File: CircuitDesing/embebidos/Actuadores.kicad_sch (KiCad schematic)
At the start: 18 parts

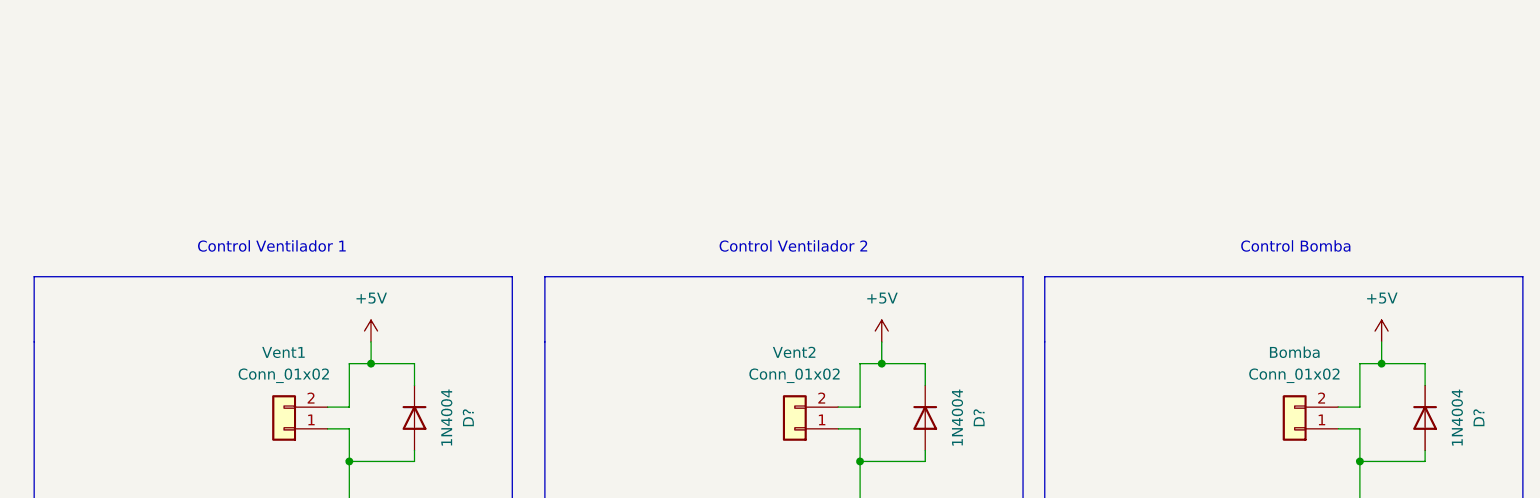
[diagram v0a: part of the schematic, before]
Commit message: Potencia
Primera propuesta del esquema de potencia
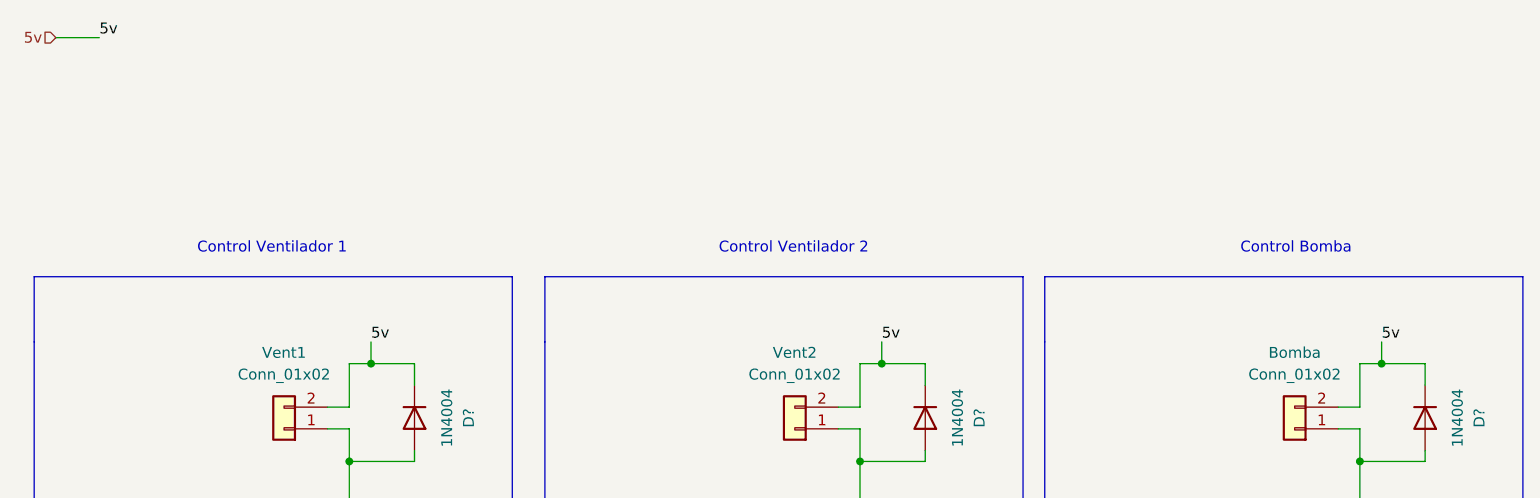
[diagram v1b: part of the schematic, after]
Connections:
- net +5V renamed 5v
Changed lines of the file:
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@@
+    (stroke (width 0) (type default) (color 0 0 0 0))
+  )
+  (wire (pts (xy 64.77 40.64) (xy 69.85 40.64))
     (stroke (width 0) (type default) (color 0 0 0 0))
   )
@@
   )
   (text "Control Ventilador 2" (at 142.24 66.04 0)
+    (effects (font (size 1.27 1.27)) (justify left bottom))
+  )
+  (label "5v" (at 161.29 76.2 0)
+    (effects (font (size 1.27 1.27)) (justify left bottom))
+  )
+  (label "5v" (at 219.71 76.2 0)
+    (effects (font (size 1.27 1.27)) (justify left bottom))
+  )
+  (label "5v" (at 101.6 76.2 0)
+    (effects (font (size 1.27 1.27)) (justify left bottom))
+  )
+  (label "5v" (at 69.85 40.64 0)
     (effects (font (size 1.27 1.27)) (justify left bottom))
   )
@@
   )
   (hierarchical_label "C_Vent2" (shape input) (at 133.35 95.25 180)
+    (effects (font (size 1.27 1.27)) (justify right))
+  )
+  (hierarchical_label "5v" (shape input) (at 64.77 40.64 180)
     (effects (font (size 1.27 1.27)) (justify right))
   )
@@
     (pin "2")
   )
-  (symbol (lib_id "power:+5V") (at 101.6 76.2 0) (unit 1)
-    (in_bom yes) (on_board yes) (fields_autoplaced)
-    (property "Reference" "#PWR?" (id 0) (at 101.6 80.01 0)
-      (effects (font (size 1.27 1.27)) hide)
-    )
-    (property "Value" "+5V" (id 1) (at 101.6 71.12 0))
-    (property "Footprint" "" (id 2) (at 101.6 76.2 0)
-      (effects (font (size 1.27 1.27)) hide)
-    )
-    (property "Datasheet" "" (id 3) (at 101.6 76.2 0)
-      (effects (font (size 1.27 1.27)) hide)
-    )
-    (pin "1")
-  )
   (symbol (lib_id "power:GND") (at 147.32 118.11 0) (unit 1)
     (in_bom yes) (on_board yes) (fields_autoplaced)
@@
     (pin "3")
   )
-  (symbol (lib_id "power:+5V") (at 219.71 76.2 0) (unit 1)
-    (in_bom yes) (on_board yes) (fields_autoplaced)
-    (property "Reference" "#PWR?" (id 0) (at 219.71 80.01 0)
-      (effects (font (size 1.27 1.27)) hide)
-    )
-    (property "Value" "+5V" (id 1) (at 219.71 71.12 0))
-    (property "Footprint" "" (id 2) (at 219.71 76.2 0)
-      (effects (font (size 1.27 1.27)) hide)
-    )
-    (property "Datasheet" "" (id 3) (at 219.71 76.2 0)
-      (effects (font (size 1.27 1.27)) hide)
-    )
-    (pin "1")
-  )
   (symbol (lib_id "Diode:1N4004") (at 106.68 85.09 270) (unit 1)
     (in_bom yes) (on_board yes) (fields_autoplaced)
@@
     (pin "2")
   )
-  (symbol (lib_id "power:+5V") (at 161.29 76.2 0) (unit 1)
-    (in_bom yes) (on_board yes) (fields_autoplaced)
-    (property "Reference" "#PWR?" (id 0) (at 161.29 80.01 0)
-      (effects (font (size 1.27 1.27)) hide)
-    )
-    (property "Value" "+5V" (id 1) (at 161.29 71.12 0))
-    (property "Footprint" "" (id 2) (at 161.29 76.2 0)
-      (effects (font (size 1.27 1.27)) hide)
-    )
-    (property "Datasheet" "" (id 3) (at 161.29 76.2 0)
-      (effects (font (size 1.27 1.27)) hide)
-    )
-    (pin "1")
-  )
   (symbol (lib_id "power:GND") (at 77.47 119.38 0) (unit 1)

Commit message: LDR
Comparacion LDR
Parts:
- R: renamed from R?; value R -> (none)
- R? (x5): value R -> (none)
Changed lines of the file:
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@@
       (effects (font (size 1.27 1.27)) (justify left))
     )
-    (property "Value" "R" (id 1) (at 90.17 107.9499 0)
+    (property "Value" "" (id 1) (at 90.17 107.9499 0)
       (effects (font (size 1.27 1.27)) (justify left))
     )
@@
   (symbol (lib_id "Device:R") (at 77.47 109.22 0) (unit 1)
     (in_bom yes) (on_board yes) (fields_autoplaced)
-    (property "Reference" "R?" (id 0) (at 80.01 107.9499 0)
-      (effects (font (size 1.27 1.27)) (justify left))
-    )
-    (property "Value" "R" (id 1) (at 80.01 110.4899 0)
+    (property "Reference" "R" (id 0) (at 80.01 107.9499 0)
+      (effects (font (size 1.27 1.27)) (justify left))
+    )
+    (property "Value" "" (id 1) (at 80.01 110.4899 0)
       (effects (font (size 1.27 1.27)) (justify left))
     )
@@
       (effects (font (size 1.27 1.27)) (justify left))
     )
-    (property "Value" "R" (id 1) (at 139.7 110.4899 0)
+    (property "Value" "" (id 1) (at 139.7 110.4899 0)
       (effects (font (size 1.27 1.27)) (justify left))
     )
@@
       (effects (font (size 1.27 1.27)) (justify left))
     )
-    (property "Value" "R" (id 1) (at 198.12 110.4899 0)
+    (property "Value" "" (id 1) (at 198.12 110.4899 0)
       (effects (font (size 1.27 1.27)) (justify left))
     )
@@
       (effects (font (size 1.27 1.27)) (justify left))
     )
-    (property "Value" "R" (id 1) (at 149.86 107.9499 0)
+    (property "Value" "" (id 1) (at 149.86 107.9499 0)
       (effects (font (size 1.27 1.27)) (justify left))
     )
@@
       (effects (font (size 1.27 1.27)) (justify left))
     )
-    (property "Value" "R" (id 1) (at 208.28 107.9499 0)
-      (effects (font (size 1.27 1.27)) (justify left))
-    )
+    (property "Value" "" (id 1) (at 208.28 107.9499 0)
+      (effects (font (size 1.27 1.27)) (justify left))
+    )

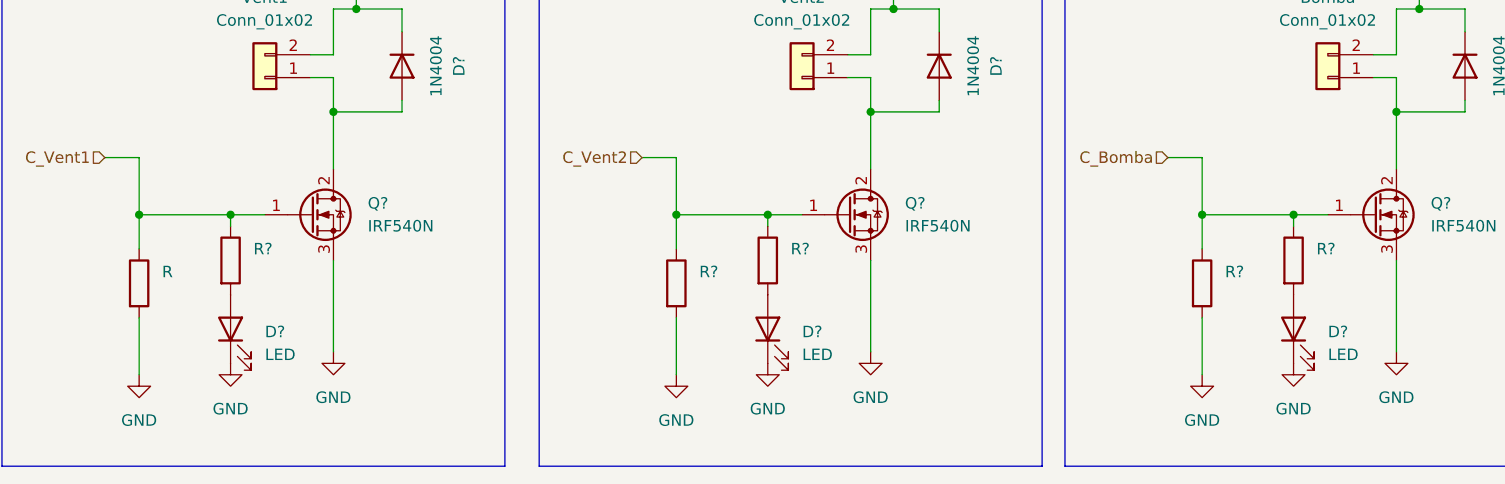
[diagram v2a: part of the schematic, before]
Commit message: Sensor Ultrasonido
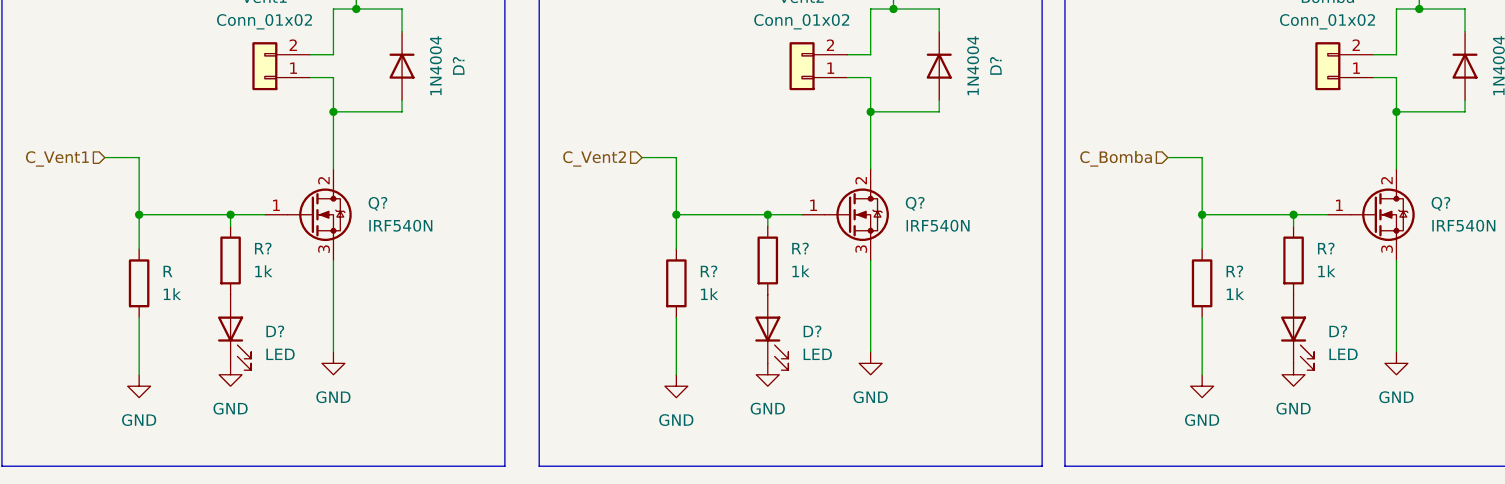
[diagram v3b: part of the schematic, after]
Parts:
- R, R? (x5): value (none) -> 1k
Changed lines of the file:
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@@
       (effects (font (size 1.27 1.27)) (justify left))
     )
-    (property "Value" "" (id 1) (at 90.17 107.9499 0)
+    (property "Value" "1k" (id 1) (at 90.17 107.9499 0)
       (effects (font (size 1.27 1.27)) (justify left))
     )
@@
       (effects (font (size 1.27 1.27)) (justify left))
     )
-    (property "Value" "" (id 1) (at 80.01 110.4899 0)
+    (property "Value" "1k" (id 1) (at 80.01 110.4899 0)
       (effects (font (size 1.27 1.27)) (justify left))
     )
@@
       (effects (font (size 1.27 1.27)) (justify left))
     )
-    (property "Value" "" (id 1) (at 139.7 110.4899 0)
+    (property "Value" "1k" (id 1) (at 139.7 110.4899 0)
       (effects (font (size 1.27 1.27)) (justify left))
     )
@@
       (effects (font (size 1.27 1.27)) (justify left))
     )
-    (property "Value" "" (id 1) (at 198.12 110.4899 0)
+    (property "Value" "1k" (id 1) (at 198.12 110.4899 0)
       (effects (font (size 1.27 1.27)) (justify left))
     )
@@
       (effects (font (size 1.27 1.27)) (justify left))
     )
-    (property "Value" "" (id 1) (at 149.86 107.9499 0)
+    (property "Value" "1k" (id 1) (at 149.86 107.9499 0)
       (effects (font (size 1.27 1.27)) (justify left))
     )
@@
       (effects (font (size 1.27 1.27)) (justify left))
     )
-    (property "Value" "" (id 1) (at 208.28 107.9499 0)
-      (effects (font (size 1.27 1.27)) (justify left))
-    )
+    (property "Value" "1k" (id 1) (at 208.28 107.9499 0)
+      (effects (font (size 1.27 1.27)) (justify left))
+    )

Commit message: Huellas parciales
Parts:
- Bomba1: renamed from Bomba; footprint (none) -> Connector_JST:JST_EH_B2B-EH-A_1x02_P2.50mm_Vertical
- gave numbers to parts that had none: 14
- renumbered R to R2
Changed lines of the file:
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@@
   (symbol (lib_id "Device:R") (at 87.63 106.68 0) (unit 1)
     (in_bom yes) (on_board yes) (fields_autoplaced)
-    (property "Reference" "R?" (id 0) (at 90.17 105.4099 0)
+    (property "Reference" "R3" (id 0) (at 90.17 105.4099 0)
       (effects (font (size 1.27 1.27)) (justify left))
     )
@@
   (symbol (lib_id "Device:LED") (at 147.32 114.3 90) (unit 1)
     (in_bom yes) (on_board yes) (fields_autoplaced)
-    (property "Reference" "D?" (id 0) (at 151.13 114.6174 90)
+    (property "Reference" "D8" (id 0) (at 151.13 114.6174 90)
       (effects (font (size 1.27 1.27)) (justify right))
     )
@@
   (symbol (lib_id "Device:R") (at 77.47 109.22 0) (unit 1)
     (in_bom yes) (on_board yes) (fields_autoplaced)
-    (property "Reference" "R" (id 0) (at 80.01 107.9499 0)
+    (property "Reference" "R2" (id 0) (at 80.01 107.9499 0)
       (effects (font (size 1.27 1.27)) (justify left))
     )
@@
   (symbol (lib_id "Transistor_FET:IRF540N") (at 96.52 101.6 0) (unit 1)
     (in_bom yes) (on_board yes) (fields_autoplaced)
-    (property "Reference" "Q?" (id 0) (at 102.87 100.3299 0)
+    (property "Reference" "Q1" (id 0) (at 102.87 100.3299 0)
       (effects (font (size 1.27 1.27)) (justify left))
     )
@@
   (symbol (lib_id "Device:LED") (at 87.63 114.3 90) (unit 1)
     (in_bom yes) (on_board yes) (fields_autoplaced)
-    (property "Reference" "D?" (id 0) (at 91.44 114.6174 90)
+    (property "Reference" "D6" (id 0) (at 91.44 114.6174 90)
       (effects (font (size 1.27 1.27)) (justify right))
     )
@@
   (symbol (lib_id "power:GND") (at 137.16 119.38 0) (unit 1)
     (in_bom yes) (on_board yes) (fields_autoplaced)
-    (property "Reference" "#PWR?" (id 0) (at 137.16 125.73 0)
+    (property "Reference" "#PWR010" (id 0) (at 137.16 125.73 0)
       (effects (font (size 1.27 1.27)) hide)
     )
@@
   (symbol (lib_id "Connector_Generic:Conn_01x02") (at 209.55 86.36 180) (unit 1)
     (in_bom yes) (on_board yes) (fields_autoplaced)
-    (property "Reference" "Bomba" (id 0) (at 209.55 77.47 0))
+    (property "Reference" "Bomba1" (id 0) (at 209.55 77.47 0))
     (property "Value" "Conn_01x02" (id 1) (at 209.55 80.01 0))
-    (property "Footprint" "" (id 2) (at 209.55 86.36 0)
+    (property "Footprint" "Connector_JST:JST_EH_B2B-EH-A_1x02_P2.50mm_Vertical" (id 2) (at 209.55 86.36 0)
       (effects (font (size 1.27 1.27)) hide)
     )
@@
   (symbol (lib_id "power:GND") (at 147.32 118.11 0) (unit 1)
     (in_bom yes) (on_board yes) (fields_autoplaced)
-    (property "Reference" "#PWR?" (id 0) (at 147.32 124.46 0)
+    (property "Reference" "#PWR011" (id 0) (at 147.32 124.46 0)
       (effects (font (size 1.27 1.27)) hide)
     )
@@
   (symbol (lib_id "Device:LED") (at 205.74 114.3 90) (unit 1)
     (in_bom yes) (on_board yes) (fields_autoplaced)
-    (property "Reference" "D?" (id 0) (at 209.55 114.6174 90)
+    (property "Reference" "D10" (id 0) (at 209.55 114.6174 90)
       (effects (font (size 1.27 1.27)) (justify right))
     )
@@
   (symbol (lib_id "power:GND") (at 87.63 118.11 0) (unit 1)
     (in_bom yes) (on_board yes) (fields_autoplaced)
-    (property "Reference" "#PWR?" (id 0) (at 87.63 124.46 0)
+    (property "Reference" "#PWR08" (id 0) (at 87.63 124.46 0)
       (effects (font (size 1.27 1.27)) hide)
     )
@@
   (symbol (lib_id "power:GND") (at 205.74 118.11 0) (unit 1)
     (in_bom yes) (on_board yes) (fields_autoplaced)
-    (property "Reference" "#PWR?" (id 0) (at 205.74 124.46 0)
+    (property "Reference" "#PWR014" (id 0) (at 205.74 124.46 0)
       (effects (font (size 1.27 1.27)) hide)
     )
@@
   (symbol (lib_id "power:GND") (at 158.75 116.84 0) (unit 1)
     (in_bom yes) (on_board yes) (fields_autoplaced)
-    (property "Reference" "#PWR?" (id 0) (at 158.75 123.19 0)
+    (property "Reference" "#PWR012" (id 0) (at 158.75 123.19 0)
       (effects (font (size 1.27 1.27)) hide)
     )
@@
   (symbol (lib_id "Transistor_FET:IRF540N") (at 156.21 101.6 0) (unit 1)
     (in_bom yes) (on_board yes) (fields_autoplaced)
-    (property "Reference" "Q?" (id 0) (at 162.56 100.3299 0)
+    (property "Reference" "Q2" (id 0) (at 162.56 100.3299 0)
       (effects (font (size 1.27 1.27)) (justify left))
     )
@@
   (symbol (lib_id "Device:R") (at 137.16 109.22 0) (unit 1)
     (in_bom yes) (on_board yes) (fields_autoplaced)
-    (property "Reference" "R?" (id 0) (at 139.7 107.9499 0)
+    (property "Reference" "R4" (id 0) (at 139.7 107.9499 0)
       (effects (font (size 1.27 1.27)) (justify left))
     )
@@
   (symbol (lib_id "Device:R") (at 195.58 109.22 0) (unit 1)
     (in_bom yes) (on_board yes) (fields_autoplaced)
-    (property "Reference" "R?" (id 0) (at 198.12 107.9499 0)
+    (property "Reference" "R6" (id 0) (at 198.12 107.9499 0)
       (effects (font (size 1.27 1.27)) (justify left))
     )
@@
   (symbol (lib_id "Diode:1N4004") (at 166.37 85.09 270) (unit 1)
     (in_bom yes) (on_board yes) (fields_autoplaced)
-    (property "Reference" "D?" (id 0) (at 172.72 85.09 0))
+    (property "Reference" "D9" (id 0) (at 172.72 85.09 0))
     (property "Value" "1N4004" (id 1) (at 170.18 85.09 0))
     (property "Footprint" "Diode_THT:D_DO-41_SOD81_P10.16mm_Horizontal" (id 2) (at 161.925 85.09 0)
@@
   (symbol (lib_id "Device:R") (at 147.32 106.68 0) (unit 1)
     (in_bom yes) (on_board yes) (fields_autoplaced)
-    (property "Reference" "R?" (id 0) (at 149.86 105.4099 0)
+    (property "Reference" "R5" (id 0) (at 149.86 105.4099 0)
       (effects (font (size 1.27 1.27)) (justify left))
     )
@@
   (symbol (lib_id "Device:R") (at 205.74 106.68 0) (unit 1)
     (in_bom yes) (on_board yes) (fields_autoplaced)
-    (property "Reference" "R?" (id 0) (at 208.28 105.4099 0)
+    (property "Reference" "R7" (id 0) (at 208.28 105.4099 0)
       (effects (font (size 1.27 1.27)) (justify left))
     )
@@
   (symbol (lib_id "power:GND") (at 195.58 119.38 0) (unit 1)
     (in_bom yes) (on_board yes) (fields_autoplaced)
-    (property "Reference" "#PWR?" (id 0) (at 195.58 125.73 0)
+    (property "Reference" "#PWR013" (id 0) (at 195.58 125.73 0)
       (effects (font (size 1.27 1.27)) hide)
     )
@@
   (symbol (lib_id "power:GND") (at 99.06 116.84 0) (unit 1)
     (in_bom yes) (on_board yes) (fields_autoplaced)
-    (property "Reference" "#PWR?" (id 0) (at 99.06 123.19 0)
+    (property "Reference" "#PWR09" (id 0) (at 99.06 123.19 0)
       (effects (font (size 1.27 1.27)) hide)
     )
@@
   (symbol (lib_id "Diode:1N4004") (at 224.79 85.09 270) (unit 1)
     (in_bom yes) (on_board yes) (fields_autoplaced)
-    (property "Reference" "D?" (id 0) (at 231.14 85.09 0))
+    (property "Reference" "D11" (id 0) (at 231.14 85.09 0))
     (property "Value" "1N4004" (id 1) (at 228.6 85.09 0))
     (property "Footprint" "Diode_THT:D_DO-41_SOD81_P10.16mm_Horizontal" (id 2) (at 220.345 85.09 0)
@@
   (symbol (lib_id "Transistor_FET:IRF540N") (at 214.63 101.6 0) (unit 1)
     (in_bom yes) (on_board yes) (fields_autoplaced)
-    (property "Reference" "Q?" (id 0) (at 220.98 100.3299 0)
+    (property "Reference" "Q3" (id 0) (at 220.98 100.3299 0)
       (effects (font (size 1.27 1.27)) (justify left))
     )
@@
   (symbol (lib_id "Diode:1N4004") (at 106.68 85.09 270) (unit 1)
     (in_bom yes) (on_board yes) (fields_autoplaced)
-    (property "Reference" "D?" (id 0) (at 113.03 85.09 0))
+    (property "Reference" "D7" (id 0) (at 113.03 85.09 0))
     (property "Value" "1N4004" (id 1) (at 110.49 85.09 0))
     (property "Footprint" "Diode_THT:D_DO-41_SOD81_P10.16mm_Horizontal" (id 2) (at 102.235 85.09 0)
@@
   (symbol (lib_id "power:GND") (at 77.47 119.38 0) (unit 1)
     (in_bom yes) (on_board yes) (fields_autoplaced)
-    (property "Reference" "#PWR?" (id 0) (at 77.47 125.73 0)
+    (property "Reference" "#PWR07" (id 0) (at 77.47 125.73 0)
       (effects (font (size 1.27 1.27)) hide)
     )
@@
   (symbol (lib_id "power:GND") (at 217.17 116.84 0) (unit 1)
     (in_bom yes) (on_board yes) (fields_autoplaced)
-    (property "Reference" "#PWR?" (id 0) (at 217.17 123.19 0)
-      (effects (font (size 1.27 1.27)) hide)
-    )
+    (property "Reference" "#PWR015" (id 0) (at 217.17 123.19 0)
+      (effects (font (size 1.27 1.27)) hide)
+    )

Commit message: 15 footprints faltantes
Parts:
- R2, R3, R4, R5, R6, R7: footprint (none) -> Resistor_SMD:R_0603_1608Metric_Pad0.98x0.95mm_HandSolder
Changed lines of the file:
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@@
       (effects (font (size 1.27 1.27)) (justify left))
     )
-    (property "Footprint" "" (id 2) (at 85.852 106.68 90)
+    (property "Footprint" "Resistor_SMD:R_0603_1608Metric_Pad0.98x0.95mm_HandSolder" (id 2) (at 85.852 106.68 90)
       (effects (font (size 1.27 1.27)) hide)
     )
@@
       (effects (font (size 1.27 1.27)) (justify left))
     )
-    (property "Footprint" "" (id 2) (at 75.692 109.22 90)
+    (property "Footprint" "Resistor_SMD:R_0603_1608Metric_Pad0.98x0.95mm_HandSolder" (id 2) (at 75.692 109.22 90)
       (effects (font (size 1.27 1.27)) hide)
     )
@@
       (effects (font (size 1.27 1.27)) (justify left))
     )
-    (property "Footprint" "" (id 2) (at 135.382 109.22 90)
+    (property "Footprint" "Resistor_SMD:R_0603_1608Metric_Pad0.98x0.95mm_HandSolder" (id 2) (at 135.382 109.22 90)
       (effects (font (size 1.27 1.27)) hide)
     )
@@
       (effects (font (size 1.27 1.27)) (justify left))
     )
-    (property "Footprint" "" (id 2) (at 193.802 109.22 90)
+    (property "Footprint" "Resistor_SMD:R_0603_1608Metric_Pad0.98x0.95mm_HandSolder" (id 2) (at 193.802 109.22 90)
       (effects (font (size 1.27 1.27)) hide)
     )
@@
       (effects (font (size 1.27 1.27)) (justify left))
     )
-    (property "Footprint" "" (id 2) (at 145.542 106.68 90)
+    (property "Footprint" "Resistor_SMD:R_0603_1608Metric_Pad0.98x0.95mm_HandSolder" (id 2) (at 145.542 106.68 90)
       (effects (font (size 1.27 1.27)) hide)
     )
@@
       (effects (font (size 1.27 1.27)) (justify left))
     )
-    (property "Footprint" "" (id 2) (at 203.962 106.68 90)
-      (effects (font (size 1.27 1.27)) hide)
-    )
+    (property "Footprint" "Resistor_SMD:R_0603_1608Metric_Pad0.98x0.95mm_HandSolder" (id 2) (at 203.962 106.68 90)
+      (effects (font (size 1.27 1.27)) hide)
+    )
